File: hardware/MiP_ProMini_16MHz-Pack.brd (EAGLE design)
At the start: 41.4 x 63.8 mm, 52 parts, among them Q1 16MHZ, U1 ATMEGA328, U2 MIC5205-5.0, U3 TS3USB221A, U4 MIC5205-3.3

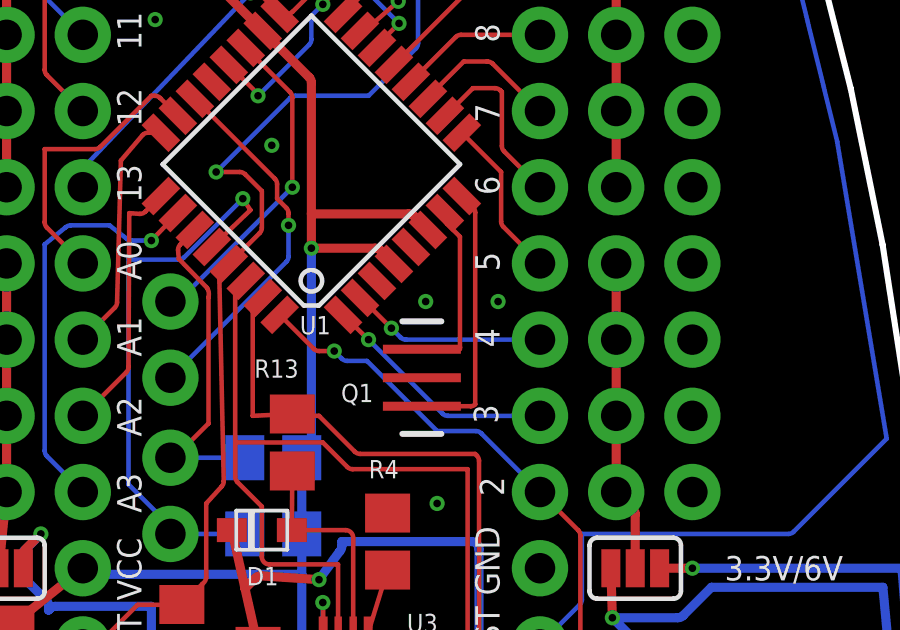
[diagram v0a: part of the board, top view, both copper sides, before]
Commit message: Update PCB design to version 4
This version update includes:
* The original Murata resonator is no longer available and the
  suggested replacement on Digikey has slightly different pad spacing.
  This commit includes BOM, documentation, and part footprint updates
  for the resonator.
* I tinted the via under R10 as I had recently shorted the bottom of
  R10 to this via by putting too much solder on the pad.

NOTE: I haven't yet had these boards made by OSHPark and tested them
      but I wanted to make these updates while they were still fresh
      in my mind.
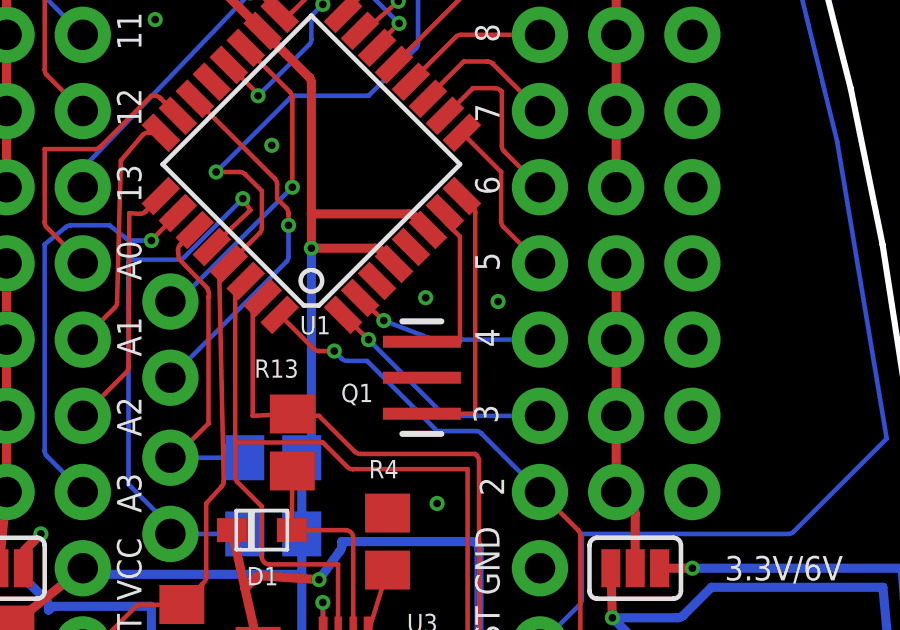
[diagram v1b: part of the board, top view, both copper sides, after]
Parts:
- Q1: device adam_custom:RESONATOR-SMD-CUSTOM -> adam_custom:RESONATOR-SMD-CUSTOM2
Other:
- board text added: "v4"
- board text removed: "v3"
